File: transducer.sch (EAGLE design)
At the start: 16 parts

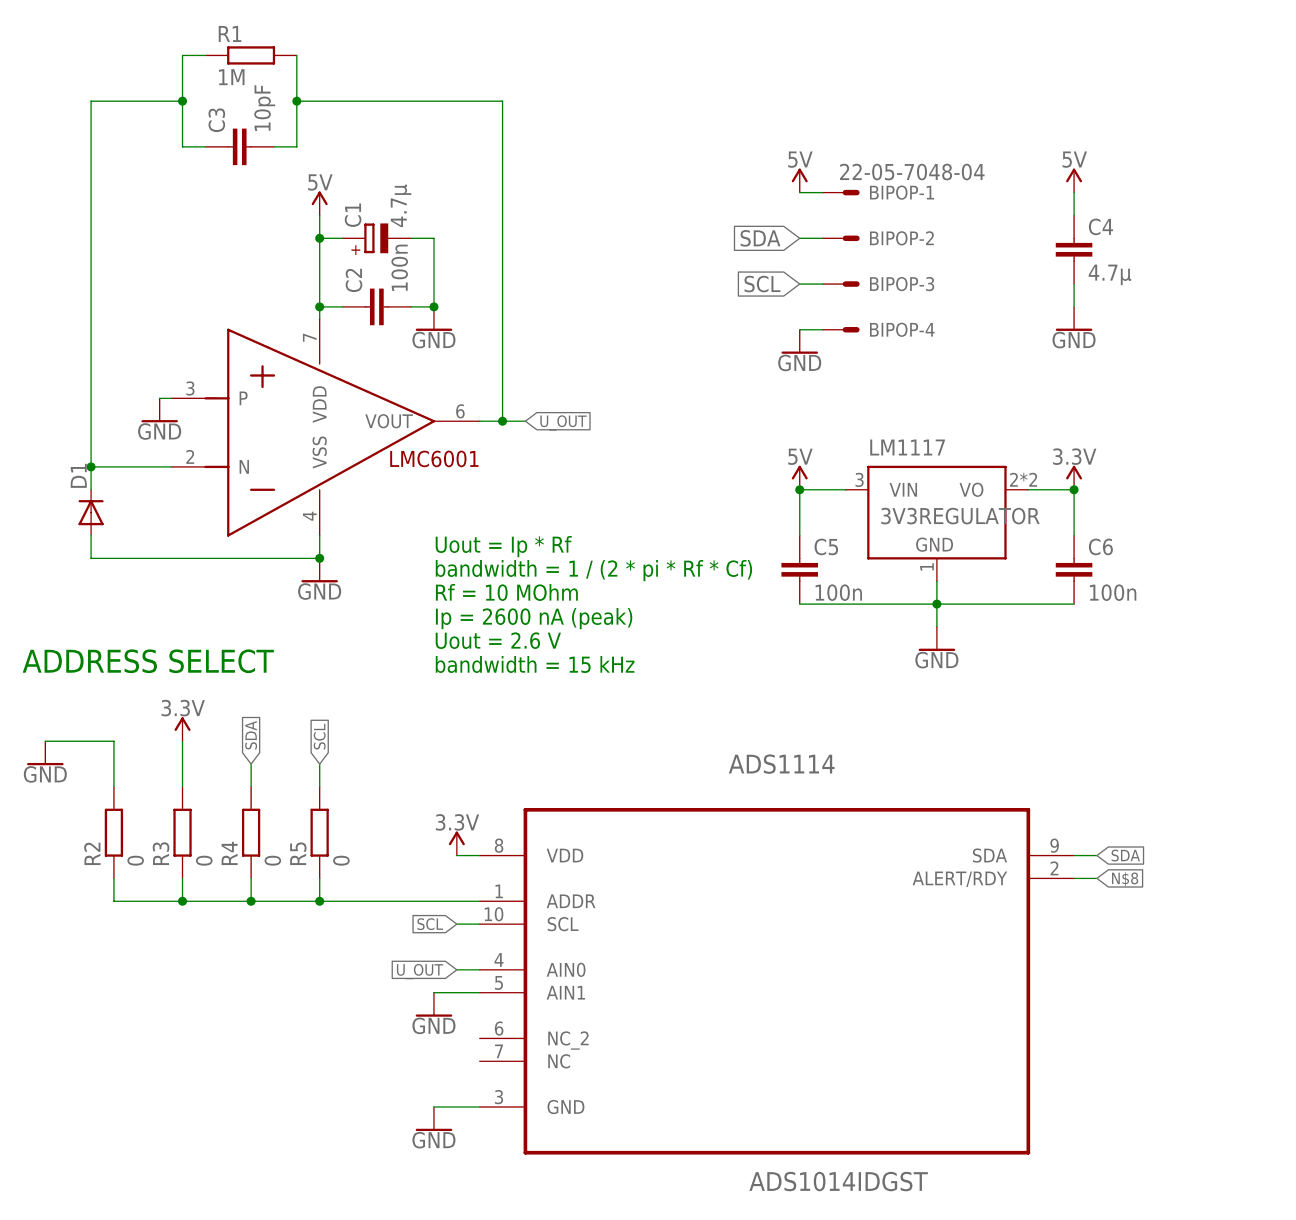
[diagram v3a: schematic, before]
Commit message: transducer redesigned - alternative
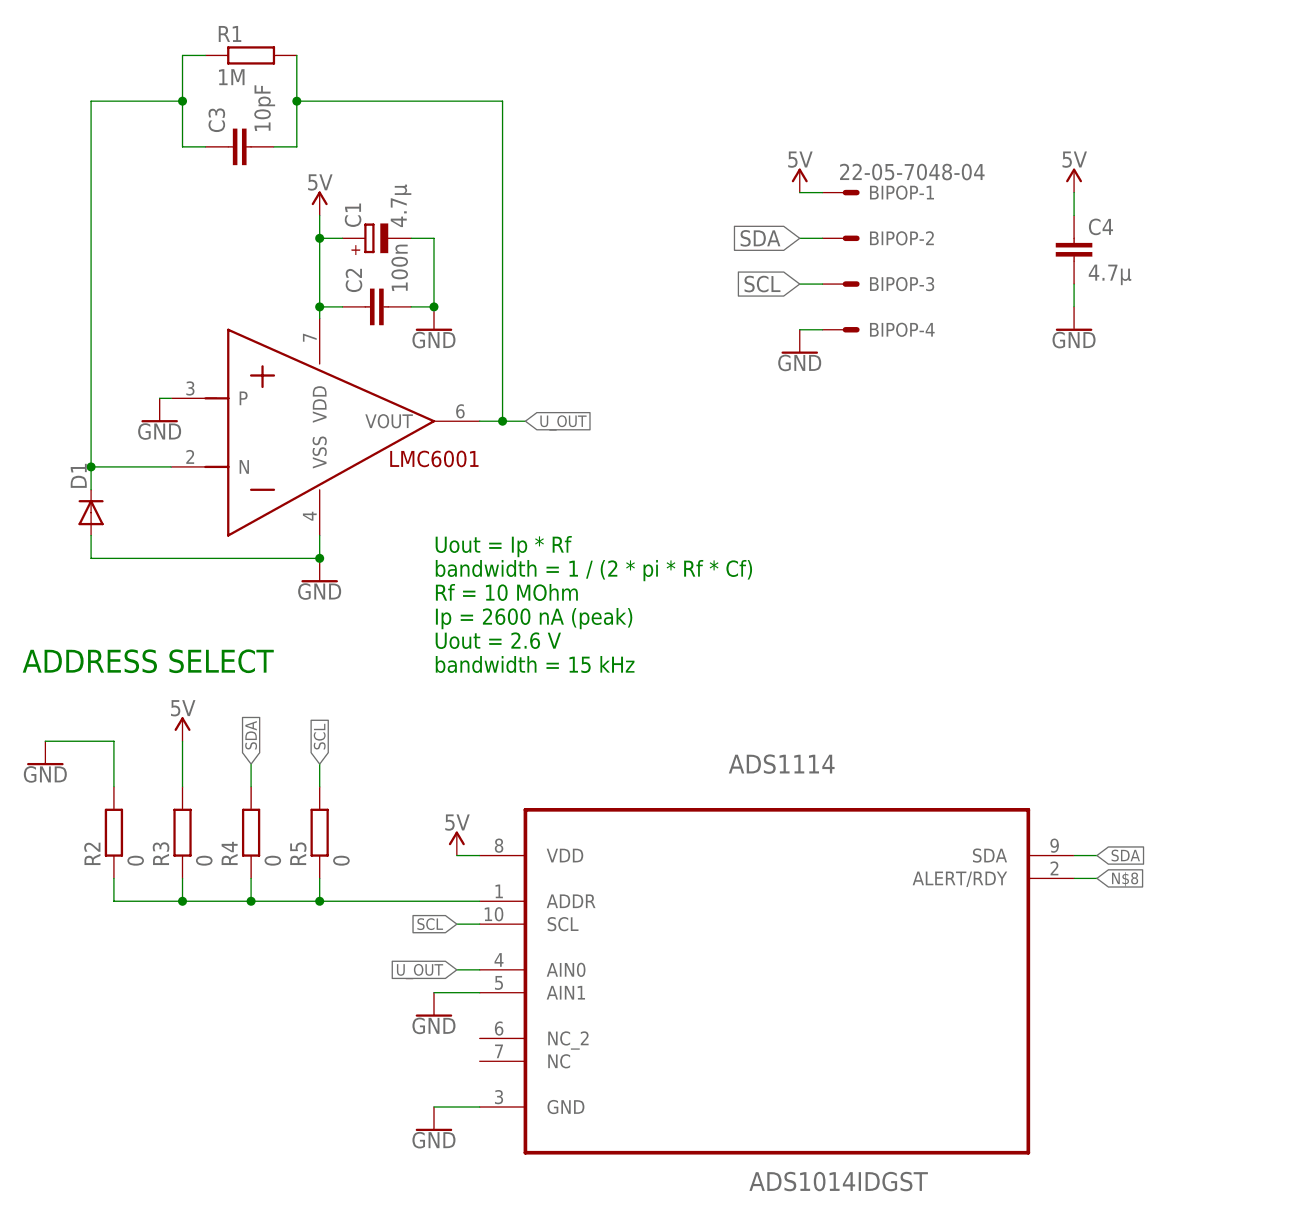
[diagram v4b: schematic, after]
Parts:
- removed C5, C6: 100n, resistor:C-EUC0805
- removed LM1117: 3V3REGULATOR, 3v3lm1117:3V3REGULATOR
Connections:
- removed net 3.3V: ADS1114.VDD, C6.1, LM1117.VO, R3.2
- net 5V: now also ADS1114.VDD, R3.2; no longer C5.1, LM1117.VIN
- net GND: no longer C5.2, C6.2, LM1117.GND
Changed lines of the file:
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@@
 <setting verticaltext="up"/>
 </settings>
-<grid distance="0.1" unitdist="inch" unit="inch" style="lines" multiple="1" display="no" altdistance="0.01" altunitdist="inch" altunit="inch"/>
+<grid distance="0.1" unitdist="inch" unit="inch" style="lines" multiple="1" display="yes" altdistance="0.01" altunitdist="inch" altunit="inch"/>
 <layers>
 <layer number="1" name="Top" color="4" fill="1" visible="no" active="no"/>
@@
 <part name="GND10" library="SparkFun-PowerSymbols" library_urn="urn:adsk.eagle:library:530" deviceset="GND" device=""/>
 <part name="C4" library="rcl" library_urn="urn:adsk.eagle:library:334" deviceset="C-EU" device="C0805" package3d_urn="urn:adsk.eagle:package:23617/2" value="4.7µ"/>
-<part name="LM1117" library="3v3lm1117" deviceset="3V3REGULATOR" device=""/>
-<part name="GND8" library="SparkFun-PowerSymbols" library_urn="urn:adsk.eagle:library:530" deviceset="GND" device=""/>
-<part name="SUPPLY3" library="SparkFun-PowerSymbols" library_urn="urn:adsk.eagle:library:530" deviceset="5V" device=""/>
-<part name="SUPPLY4" library="SparkFun-PowerSymbols" library_urn="urn:adsk.eagle:library:530" deviceset="3.3V" device=""/>
-<part name="SUPPLY6" library="SparkFun-PowerSymbols" library_urn="urn:adsk.eagle:library:530" deviceset="3.3V" device=""/>
-<part name="SUPPLY7" library="SparkFun-PowerSymbols" library_urn="urn:adsk.eagle:library:530" deviceset="3.3V" device=""/>
-<part name="C5" library="resistor" library_urn="urn:adsk.eagle:library:348" deviceset="C-EU" device="C0805" package3d_urn="urn:adsk.eagle:package:26137/1" value="100n"/>
-<part name="C6" library="resistor" library_urn="urn:adsk.eagle:library:348" deviceset="C-EU" device="C0805" package3d_urn="urn:adsk.eagle:package:26137/1" value="100n"/>
+<part name="SUPPLY6" library="SparkFun-PowerSymbols" library_urn="urn:adsk.eagle:library:530" deviceset="5V" device=""/>
+<part name="SUPPLY7" library="SparkFun-PowerSymbols" library_urn="urn:adsk.eagle:library:530" deviceset="5V" device=""/>
 </parts>
 <sheets>
@@
 <instance part="GND10" gate="1" x="139.7" y="60.96"/>
 <instance part="C4" gate="G$1" x="139.7" y="71.12"/>
-<instance part="LM1117" gate="G$1" x="124.46" y="40.64"/>
-<instance part="GND8" gate="1" x="124.46" y="25.4"/>
-<instance part="SUPPLY3" gate="G$1" x="109.22" y="43.18"/>
-<instance part="SUPPLY4" gate="G$1" x="139.7" y="43.18"/>
 <instance part="SUPPLY6" gate="G$1" x="40.64" y="15.24"/>
 <instance part="SUPPLY7" gate="G$1" x="71.12" y="2.54"/>
-<instance part="C5" gate="G$1" x="109.22" y="35.56"/>
-<instance part="C6" gate="G$1" x="139.7" y="35.56"/>
 </instances>
 <busses>
 </busses>
 <nets>
-<net name="SDA" class="0">
-<segment>
-<pinref part="BIPOP" gate="-2" pin="S"/>
-<wire x1="111.76" y1="71.12" x2="109.22" y2="71.12" width="0.1524" layer="91"/>
-<label x="109.22" y="71.12" size="1.778" layer="95" rot="R180" xref="yes"/>
-</segment>
-<segment>
-<pinref part="ADS1114" gate="A" pin="SDA"/>
-<wire x1="139.7" y1="2.54" x2="142.24" y2="2.54" width="0.1524" layer="91"/>
-<label x="142.24" y="2.54" size="1.27" layer="95" xref="yes"/>
-</segment>
-<segment>
-<wire x1="48.26" y1="12.7" x2="48.26" y2="10.16" width="0.1524" layer="91"/>
-<label x="48.26" y="12.7" size="1.27" layer="95" rot="R90" xref="yes"/>
-<pinref part="R4" gate="G$1" pin="2"/>
-</segment>
-</net>
-<net name="SCL" class="0">
-<segment>
-<pinref part="BIPOP" gate="-3" pin="S"/>
-<wire x1="111.76" y1="66.04" x2="109.22" y2="66.04" width="0.1524" layer="91"/>
-<label x="109.22" y="66.04" size="1.778" layer="95" rot="R180" xref="yes"/>
-</segment>
-<segment>
-<pinref part="ADS1114" gate="A" pin="SCL"/>
-<wire x1="73.66" y1="-5.08" x2="71.12" y2="-5.08" width="0.1524" layer="91"/>
-<label x="71.12" y="-5.08" size="1.27" layer="95" rot="R180" xref="yes"/>
-</segment>
-<segment>
-<wire x1="55.88" y1="12.7" x2="55.88" y2="10.16" width="0.1524" layer="91"/>
-<label x="55.88" y="12.7" size="1.27" layer="95" rot="R90" xref="yes"/>
-<pinref part="R5" gate="G$1" pin="2"/>
-</segment>
-</net>
 <net name="GND" class="0">
 <segment>
@@
 <pinref part="GND10" gate="1" pin="GND"/>
 <wire x1="139.7" y1="66.04" x2="139.7" y2="63.5" width="0.1524" layer="91"/>
-</segment>
-<segment>
-<pinref part="LM1117" gate="G$1" pin="GND"/>
-<pinref part="GND8" gate="1" pin="GND"/>
-<wire x1="124.46" y1="27.94" x2="124.46" y2="30.48" width="0.1524" layer="91"/>
-<pinref part="C6" gate="G$1" pin="2"/>
-<wire x1="124.46" y1="30.48" x2="124.46" y2="33.02" width="0.1524" layer="91"/>
-<wire x1="139.7" y1="30.48" x2="124.46" y2="30.48" width="0.1524" layer="91"/>
-<junction x="124.46" y="30.48"/>
-<pinref part="C5" gate="G$1" pin="2"/>
-<wire x1="109.22" y1="30.48" x2="124.46" y2="30.48" width="0.1524" layer="91"/>
 </segment>
 </net>
@@
 </segment>
 <segment>
-<pinref part="LM1117" gate="G$1" pin="VIN"/>
-<pinref part="SUPPLY3" gate="G$1" pin="5V"/>
-<wire x1="109.22" y1="43.18" x2="114.3" y2="43.18" width="0.1524" layer="91"/>
-<pinref part="C5" gate="G$1" pin="1"/>
-<wire x1="109.22" y1="43.18" x2="109.22" y2="38.1" width="0.1524" layer="91"/>
-<junction x="109.22" y="43.18"/>
-</segment>
-</net>
-<net name="3.3V" class="0">
-<segment>
-<pinref part="LM1117" gate="G$1" pin="VO"/>
-<pinref part="SUPPLY4" gate="G$1" pin="3.3V"/>
-<wire x1="139.7" y1="43.18" x2="134.62" y2="43.18" width="0.1524" layer="91"/>
-<pinref part="C6" gate="G$1" pin="1"/>
-<wire x1="139.7" y1="43.18" x2="139.7" y2="38.1" width="0.1524" layer="91"/>
-<junction x="139.7" y="43.18"/>
-</segment>
-<segment>
 <pinref part="R3" gate="G$1" pin="2"/>
-<pinref part="SUPPLY6" gate="G$1" pin="3.3V"/>
 <wire x1="40.64" y1="15.24" x2="40.64" y2="10.16" width="0.1524" layer="91"/>
+<pinref part="SUPPLY6" gate="G$1" pin="5V"/>
 </segment>
 <segment>
 <pinref part="ADS1114" gate="A" pin="VDD"/>
 <wire x1="73.66" y1="2.54" x2="71.12" y2="2.54" width="0.1524" layer="91"/>
-<pinref part="SUPPLY7" gate="G$1" pin="3.3V"/>
-</segment>
-</net>
+<pinref part="SUPPLY7" gate="G$1" pin="5V"/>
+</segment>
+</net>
+<net name="SDA" class="0">
+<segment>
+<pinref part="BIPOP" gate="-2" pin="S"/>
+<wire x1="111.76" y1="71.12" x2="109.22" y2="71.12" width="0.1524" layer="91"/>
+<label x="109.22" y="71.12" size="1.778" layer="95" rot="R180" xref="yes"/>
+</segment>
+<segment>
+<wire x1="48.26" y1="12.7" x2="48.26" y2="10.16" width="0.1524" layer="91"/>
+<label x="48.26" y="12.7" size="1.27" layer="95" rot="R90" xref="yes"/>
+<pinref part="R4" gate="G$1" pin="2"/>
+</segment>
+<segment>
+<pinref part="ADS1114" gate="A" pin="SDA"/>
+<wire x1="139.7" y1="2.54" x2="142.24" y2="2.54" width="0.1524" layer="91"/>
+<label x="142.24" y="2.54" size="1.27" layer="95" xref="yes"/>
+</segment>
+</net>
+<net name="SCL" class="0">
+<segment>
+<pinref part="BIPOP" gate="-3" pin="S"/>
+<wire x1="111.76" y1="66.04" x2="109.22" y2="66.04" width="0.1524" layer="91"/>
+<label x="109.22" y="66.04" size="1.778" layer="95" rot="R180" xref="yes"/>
+</segment>
+<segment>
+<wire x1="55.88" y1="12.7" x2="55.88" y2="10.16" width="0.1524" layer="91"/>
+<label x="55.88" y="12.7" size="1.27" layer="95" rot="R90" xref="yes"/>
+<pinref part="R5" gate="G$1" pin="2"/>
+</segment>
+<segment>
+<pinref part="ADS1114" gate="A" pin="SCL"/>
+<wire x1="73.66" y1="-5.08" x2="71.12" y2="-5.08" width="0.1524" layer="91"/>
+<label x="71.12" y="-5.08" size="1.27" layer="95" rot="R180" xref="yes"/>
+</segment>
+</net>
